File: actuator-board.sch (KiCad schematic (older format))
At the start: 27 parts, among them U1 STM32F302K8U6, U2 MCP1703, U3 MAX3051, X1 16MHz 10ppm

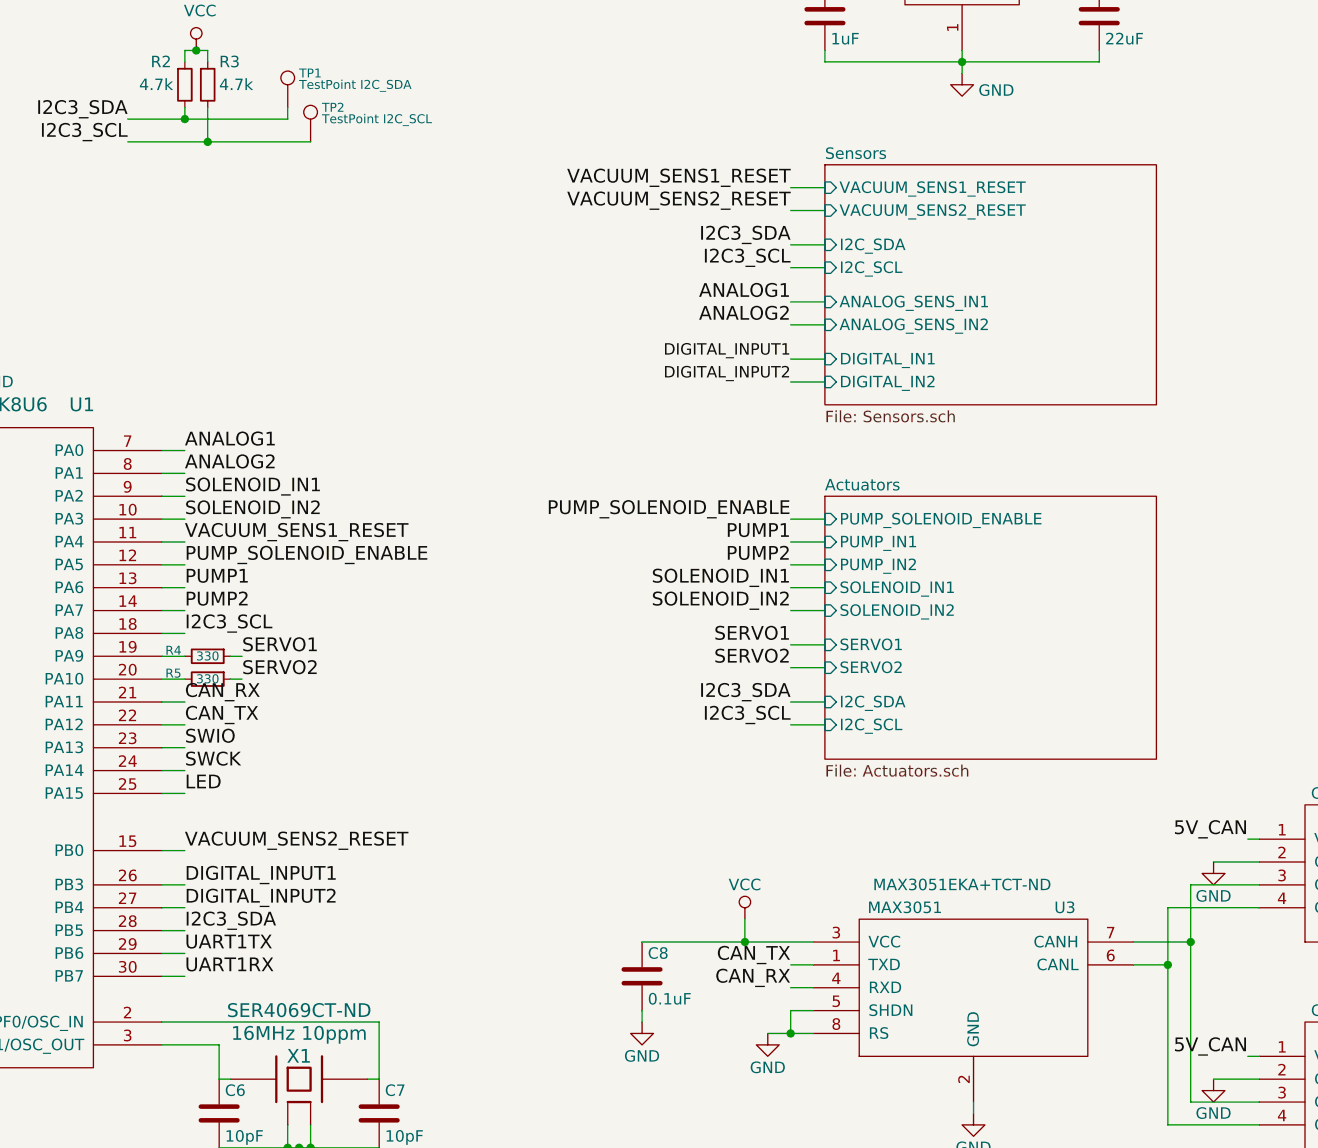
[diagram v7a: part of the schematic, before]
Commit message: Switch to SPI, fixed sensor and motor driver symbols.
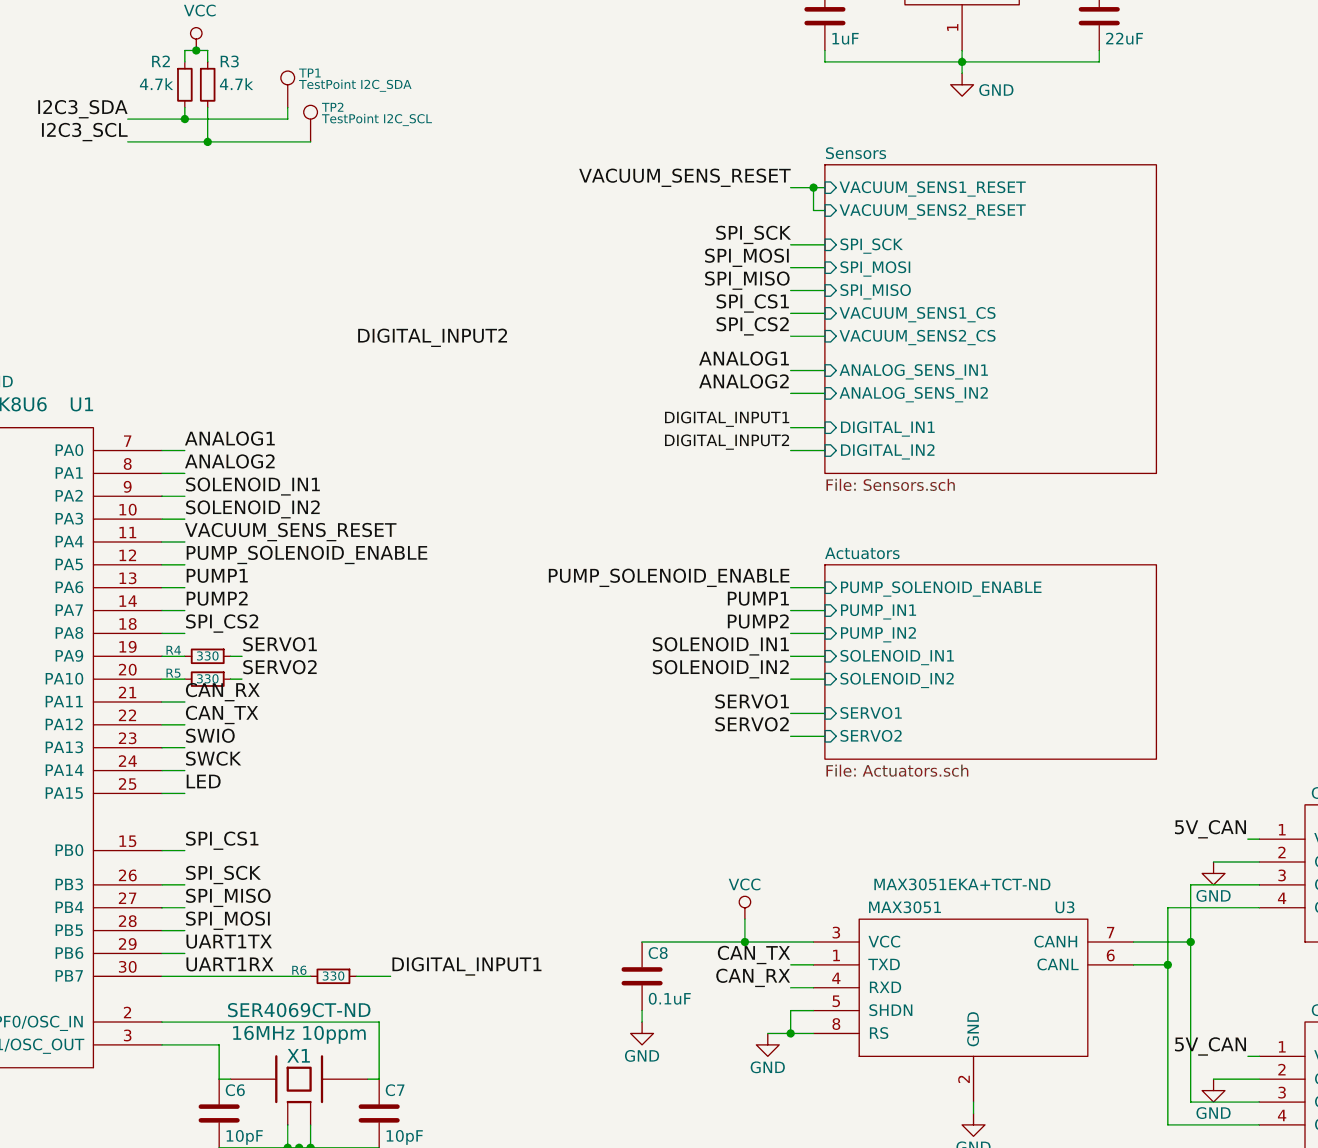
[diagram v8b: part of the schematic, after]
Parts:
- added R6: 330, symbol Device:R_Small
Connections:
- net DIGITAL_INPUT1: now also R6.1; no longer U1.26 (PB3)
- net DIGITAL_INPUT2: no longer U1.27 (PB4)
- net I2C3_SCL: no longer U1.18 (PA8)
- net I2C3_SDA: no longer U1.28 (PB5)
- net UART1RX: now also R6.2
- net VACUUM_SENS1_RESET renamed VACUUM_SENS_RESET
- net VACUUM_SENS2_RESET renamed SPI_CS1
- new net SPI_CS2: U1.18 (PA8)
- new net SPI_MISO: U1.27 (PB4)
- new net SPI_MOSI: U1.28 (PB5)
- new net SPI_SCK: U1.26 (PB3)
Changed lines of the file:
@@
 Text Notes 9250 850  0    60   ~ 0
 3.3V
-Text Label 8100 3950 2    60   ~ 0
+Text Label 8100 4250 2    60   ~ 0
 SERVO1
-Text Label 8100 3400 2    60   ~ 0
+Text Label 8100 3700 2    60   ~ 0
 PUMP_SOLENOID_ENABLE
 Wire Wire Line
 	9850 5000 10150 5000
-Text Label 8100 3500 2    60   ~ 0
+Text Label 8100 3800 2    60   ~ 0
 PUMP1
-Text Label 8100 3600 2    60   ~ 0
+Text Label 8100 3900 2    60   ~ 0
 PUMP2
 Text Label 5450 3600 0    60   ~ 0
 PUMP_SOLENOID_ENABLE
-Text Label 5450 5200 0    60   ~ 0
-I2C3_SDA
-Text Label 8100 4050 2    60   ~ 0
+Text Label 8100 4350 2    60   ~ 0
 SERVO2
-Text Label 5450 3900 0    60   ~ 0
-I2C3_SCL
-Text Label 8100 2550 2    60   ~ 0
+Text Label 8100 2850 2    60   ~ 0
 ANALOG2
-Text Label 8100 4200 2    60   ~ 0
-I2C3_SDA
-Text Label 8100 4300 2    60   ~ 0
-I2C3_SCL
-Text Label 8100 2450 2    60   ~ 0
+Text Label 8100 2750 2    60   ~ 0
 ANALOG1
 Text Label 8100 1950 2    60   ~ 0
-VACUUM_SENS1_RESET
+VACUUM_SENS_RESET
 $Comp
 L _connectors:PWR CONN2
@@
 	1    0    0    -1
 $EndComp
-Text Label 8100 2300 2    60   ~ 0
-I2C3_SCL
-Text Label 8100 2200 2    60   ~ 0
-I2C3_SDA
 Connection ~ 3500 4200
 Wire Wire Line
@@
 UART1RX
 Wire Wire Line
-	5450 5400 5350 5400
-Wire Wire Line
 	5350 5200 5450 5200
 Wire Wire Line
 	5350 3900 5450 3900
 Text Label 5450 3500 0    60   ~ 0
-VACUUM_SENS1_RESET
-Text Label 8100 2700 2    50   ~ 0
+VACUUM_SENS_RESET
+Text Label 8100 3000 2    50   ~ 0
 DIGITAL_INPUT1
 Wire Wire Line
@@
 Wire Wire Line
 	1750 1500 2150 1500
-Text Label 8100 2050 2    60   ~ 0
-VACUUM_SENS2_RESET
 $Sheet
-S 8250 1850 1450 1050
+S 8250 1850 1450 1350
 U 5E1FAFCF
 F0 "Sensors" 50
 F1 "Sensors.sch" 50
 F2 "VACUUM_SENS1_RESET" I L 8250 1950 50
-F3 "ANALOG_SENS_IN1" I L 8250 2450 50
-F4 "ANALOG_SENS_IN2" I L 8250 2550 50
-F5 "I2C_SDA" I L 8250 2200 50
-F6 "I2C_SCL" I L 8250 2300 50
-F7 "DIGITAL_IN1" I L 8250 2700 50
-F8 "DIGITAL_IN2" I L 8250 2800 50
-F9 "VACUUM_SENS2_RESET" I L 8250 2050 50
+F3 "ANALOG_SENS_IN1" I L 8250 2750 50
+F4 "ANALOG_SENS_IN2" I L 8250 2850 50
+F5 "DIGITAL_IN1" I L 8250 3000 50
+F6 "DIGITAL_IN2" I L 8250 3100 50
+F7 "VACUUM_SENS2_RESET" I L 8250 2050 50
+F8 "SPI_SCK" I L 8250 2200 50
+F9 "SPI_MOSI" I L 8250 2300 50
+F10 "SPI_MISO" I L 8250 2400 50
+F11 "VACUUM_SENS1_CS" I L 8250 2500 50
+F12 "VACUUM_SENS2_CS" I L 8250 2600 50
 $EndSheet
 $Sheet
-S 8250 3300 1450 1150
+S 8250 3600 1450 850
 U 5E1FB153
 F0 "Actuators" 50
 F1 "Actuators.sch" 50
-F2 "PUMP_IN1" I L 8250 3500 50
-F3 "PUMP_IN2" I L 8250 3600 50
-F4 "SERVO1" I L 8250 3950 50
-F5 "SERVO2" I L 8250 4050 50
-F6 "I2C_SDA" I L 8250 4200 50
-F7 "I2C_SCL" I L 8250 4300 50
-F8 "PUMP_SOLENOID_ENABLE" I L 8250 3400 50
-F9 "SOLENOID_IN1" I L 8250 3700 50
-F10 "SOLENOID_IN2" I L 8250 3800 50
+F2 "PUMP_IN1" I L 8250 3800 50
+F3 "PUMP_IN2" I L 8250 3900 50
+F4 "SERVO1" I L 8250 4250 50
+F5 "SERVO2" I L 8250 4350 50
+F6 "PUMP_SOLENOID_ENABLE" I L 8250 3700 50
+F7 "SOLENOID_IN1" I L 8250 4000 50
+F8 "SOLENOID_IN2" I L 8250 4100 50
 $EndSheet
-Text Label 8100 3700 2    60   ~ 0
+Text Label 8100 4000 2    60   ~ 0
 SOLENOID_IN1
-Text Label 8100 3800 2    60   ~ 0
+Text Label 8100 4100 2    60   ~ 0
 SOLENOID_IN2
 Connection ~ 3850 4000
@@
 Wire Wire Line
 	5350 3600 5450 3600
-Text Label 5450 5000 0    60   ~ 0
-DIGITAL_INPUT1
-Text Label 5450 5100 0    60   ~ 0
+Text Label 6200 2650 0    60   ~ 0
 DIGITAL_INPUT2
-Text Label 8100 2800 2    50   ~ 0
+Text Label 8100 3100 2    50   ~ 0
 DIGITAL_INPUT2
 Wire Wire Line
@@
 Wire Wire Line
 	5450 5000 5350 5000
-Text Label 5450 4850 0    60   ~ 0
-VACUUM_SENS2_RESET
 Wire Wire Line
 	5350 4850 5450 4850
@@
 	5650 4100 5700 4100
 Wire Wire Line
-	8100 3400 8250 3400
-Wire Wire Line
-	8100 3500 8250 3500
-Wire Wire Line
-	8100 3600 8250 3600
-Wire Wire Line
 	8100 3700 8250 3700
 Wire Wire Line
 	8100 3800 8250 3800
 Wire Wire Line
-	8100 3950 8250 3950
-Wire Wire Line
-	8100 4050 8250 4050
-Wire Wire Line
-	8100 4200 8250 4200
-Wire Wire Line
-	8100 4300 8250 4300
-Wire Wire Line
-	8100 1950 8250 1950
-Wire Wire Line
-	8100 2050 8250 2050
-Wire Wire Line
-	8250 2200 8100 2200
-Wire Wire Line
-	8100 2300 8250 2300
-Wire Wire Line
-	8250 2450 8100 2450
-Wire Wire Line
-	8100 2550 8250 2550
-Wire Wire Line
-	8250 2700 8100 2700
-Wire Wire Line
-	8100 2800 8250 2800
+	8100 3900 8250 3900
+Wire Wire Line
+	8100 4000 8250 4000
+Wire Wire Line
+	8100 4100 8250 4100
+Wire Wire Line
+	8100 4250 8250 4250
+Wire Wire Line
+	8100 4350 8250 4350
+Wire Wire Line
+	8250 2750 8100 2750
+Wire Wire Line
+	8100 2850 8250 2850
+Wire Wire Line
+	8250 3000 8100 3000
+Wire Wire Line
+	8100 3100 8250 3100
 $Comp
 L Device:R_Small R2
@@
 Wire Wire Line
 	5900 1600 5900 1650
+Text Label 6350 5400 0    60   ~ 0
+DIGITAL_INPUT1
+Text Label 5450 5200 0    60   ~ 0
+SPI_MOSI
+Text Label 5450 5100 0    60   ~ 0
+SPI_MISO
+Text Label 5450 5000 0    60   ~ 0
+SPI_SCK
+Text Label 5450 4850 0    60   ~ 0
+SPI_CS1
+Text Label 5450 3900 0    60   ~ 0
+SPI_CS2
+$Comp
+L Device:R_Small R6
+U 1 1 5E3D0925
+P 6100 5400
+F 0 "R6" V 6075 5250 39  0000 C CNN
+F 1 "330" V 6100 5400 39  0000 C CNN
+F 2 "" H 6100 5400 50  0001 C CNN
+F 3 "~" H 6100 5400 50  0001 C CNN
+	1    6100 5400
+	0    1    1    0
+$EndComp
+Wire Wire Line
+	6200 5400 6350 5400
+Wire Wire Line
+	5350 5400 6000 5400
+Text Label 8100 2600 2    60   ~ 0
+SPI_CS2
+Text Label 8100 2500 2    60   ~ 0
+SPI_CS1
+Text Label 8100 2200 2    60   ~ 0
+SPI_SCK
+Wire Wire Line
+	8100 2200 8250 2200
+Text Label 8100 2400 2    60   ~ 0
+SPI_MISO
+Text Label 8100 2300 2    60   ~ 0
+SPI_MOSI
+Wire Wire Line
+	8100 2300 8250 2300
+Wire Wire Line
+	8250 2400 8100 2400
+Wire Wire Line
+	8100 2500 8250 2500
+Wire Wire Line
+	8250 2600 8100 2600
+Wire Wire Line
+	8200 2050 8250 2050
+Wire Wire Line
+	8200 1950 8250 1950
+Connection ~ 8200 1950
+Wire Wire Line
+	8200 2050 8200 1950
+Wire Wire Line
+	8100 1950 8200 1950
 $EndSCHEMATC
